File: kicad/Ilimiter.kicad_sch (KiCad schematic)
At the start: 6 parts, among them Q3 NPN

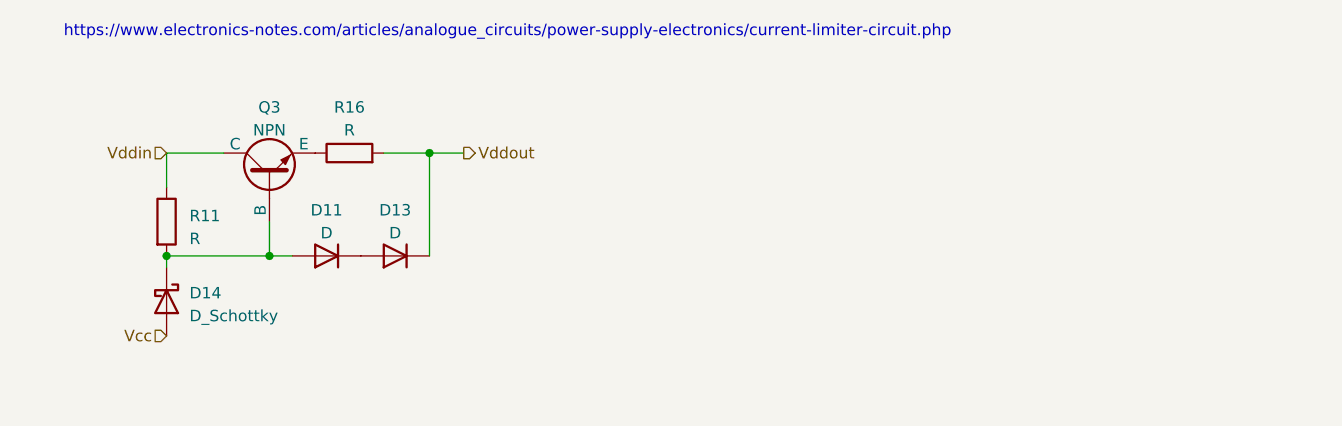
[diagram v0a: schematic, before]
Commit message: Subdivide circuits into hierarchical sheets
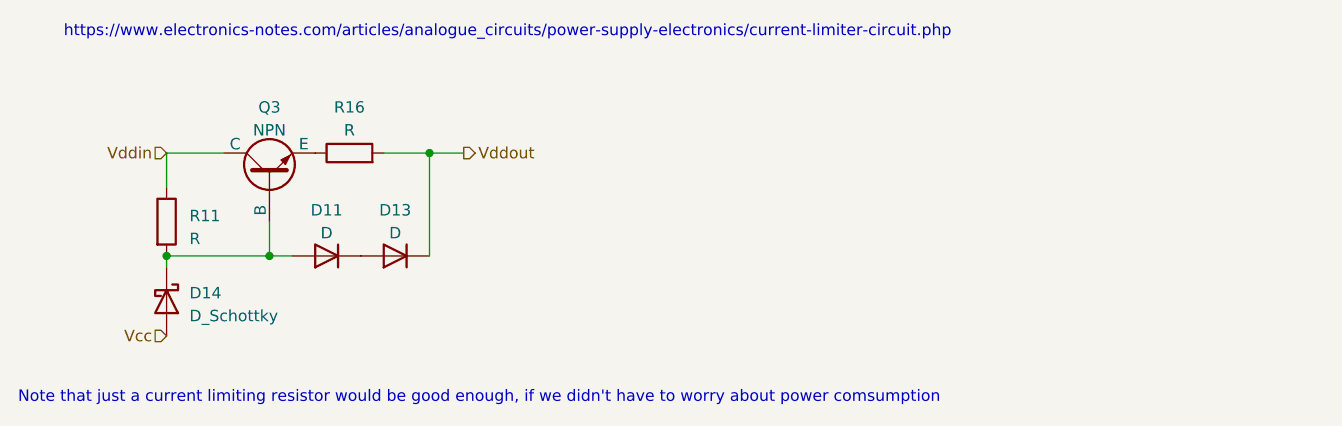
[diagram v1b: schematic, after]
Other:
- note added: "Note that just a current limiting resistor would be good enough, if we didn't have to worry about power comsumption"
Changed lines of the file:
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@@
+    (effects (font (size 1.27 1.27)) (justify left bottom))
+  )
+  (text "Note that just a current limiting resistor would be good enough, if we didn't have to worry about power comsumption"
+    (at 57.15 110.49 0)
     (effects (font (size 1.27 1.27)) (justify left bottom))
   )
